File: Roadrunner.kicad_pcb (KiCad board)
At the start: 4 copper layers, 68.6 x 52.1 mm, 100 parts, among them J1 USB_OTG, J10 Digital, J11 ~WAKE, J13 SERIAL 4, J14 SERIAL 3, J15 -AREF, J16 +AREF, J17 SPI 2 (D22,D23), J19 SERIAL 2, J2 JTAG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

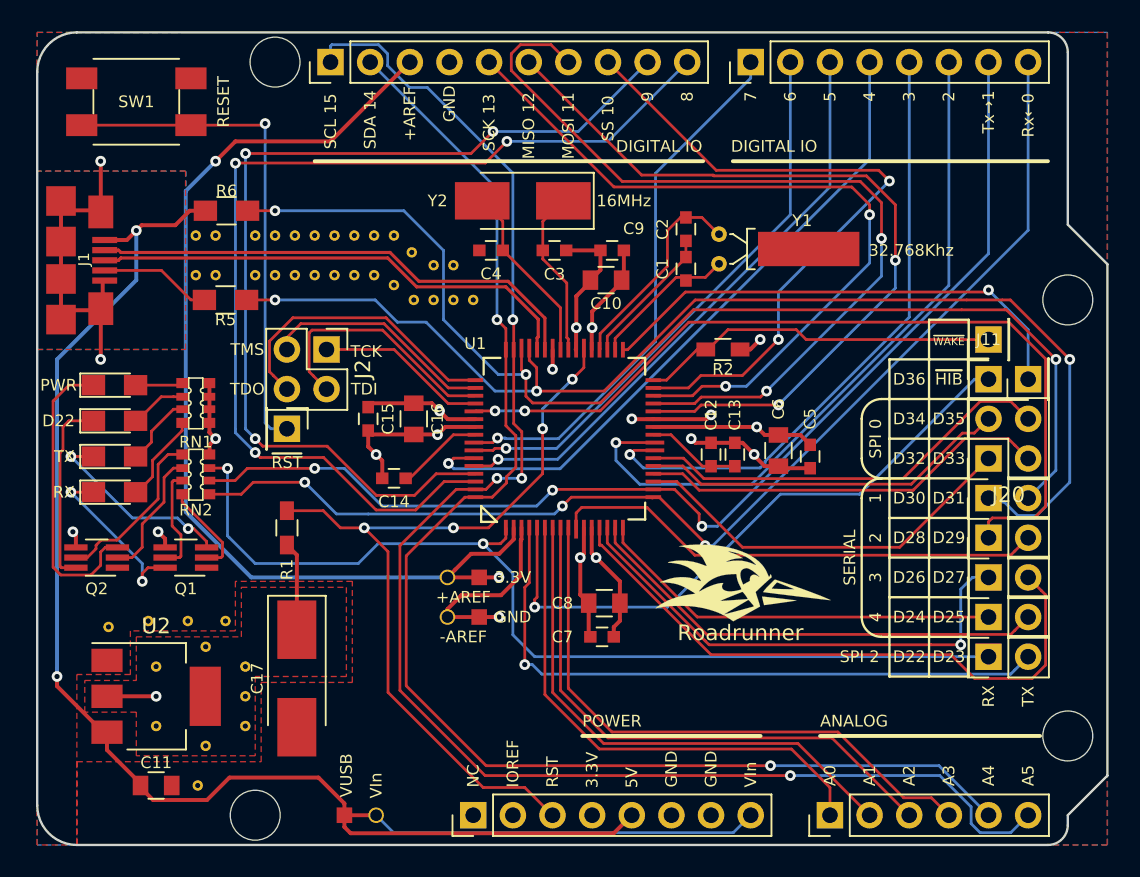
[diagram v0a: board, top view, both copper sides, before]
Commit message: Renaming project ro Roadrunner
Also include various routing changes and a new logo
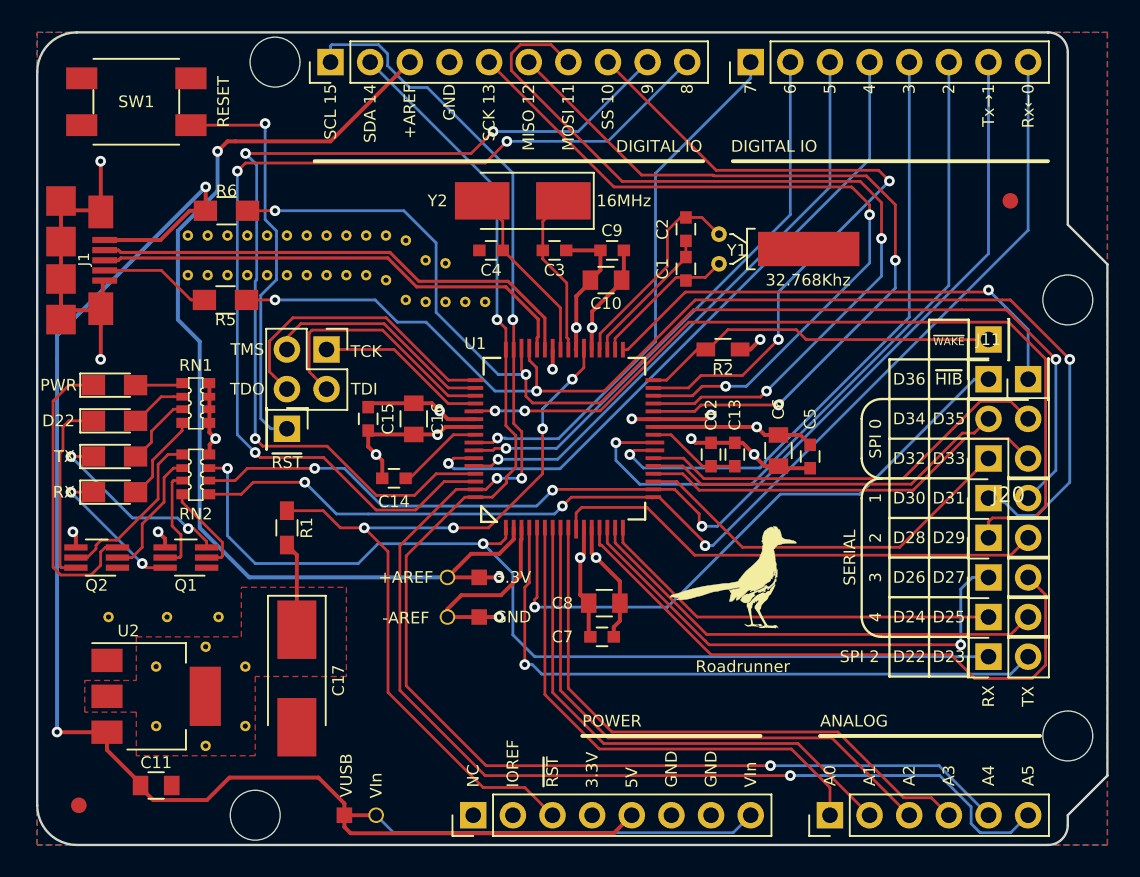
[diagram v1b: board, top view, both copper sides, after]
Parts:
- removed G***: LOGO, Custom-Mounting-Holes:My_Roadrunner
- removed G***: LOGO, Custom-Mounting-Holes:My_Roadrunner_smaller
- removed the REF** at (120.7, 111.4)
- removed the REF** at (127.5, 86.7)
- removed the REF** at (126.2, 89.2)
- removed the REF** at (123.1, 111.4)
- removed the REF** at (121.3, 121.9)
- removed the REF** at (124.3, 116.2)
- added REF**: Fiducial_1mm_Dia_2.54mm_Outer_CopperTop, Fiducials:Fiducial_1mm_Dia_2.54mm_Outer_CopperTop, F.Cu at (173.4, 84.5)
- added REF**: VIA-0.33mm, Custom-Mounting-Holes:VIA-0.33mm, F.Cu at (122.6, 111.1)
- added REF**: VIA-0.33mm, Custom-Mounting-Holes:VIA-0.33mm, F.Cu at (124.5, 86.7)
- added REF**: VIA-0.33mm, Custom-Mounting-Holes:VIA-0.33mm, F.Cu at (123.2, 86.7)
- added REF**: Fiducial_1mm_Dia_2.54mm_Outer_CopperTop, Fiducials:Fiducial_1mm_Dia_2.54mm_Outer_CopperTop, F.Cu at (113.7, 123.2)
- added REF**: VIA-0.33mm, Custom-Mounting-Holes:VIA-0.33mm, F.Cu at (123.2, 89.2)
- added REF**: VIA-0.33mm, Custom-Mounting-Holes:VIA-0.33mm, F.Cu at (124.5, 89.2)
- added REF**: VIA-0.33mm, Custom-Mounting-Holes:VIA-0.33mm, F.Cu at (139.7, 90.9)
- added RoadrunnerLogoMedium: G***, Project-Symbols_Local:RoadrunnerLogoMedium, B.Cu at (128.9, 99.7)
- added RoadrunnerLogoSmall: G***, Project-Symbols_Local:RoadrunnerLogoSmall, F.Cu at (155.6, 108.6)
- moved REF** 1.23 mm to (119.3, 111.1)
- moved REF** 0.85 mm to (134.6, 87.0)
- moved REF** 0.76 mm to (125.7, 86.7)
- moved REF** 0.76 mm to (125.7, 89.2)
- moved REF** 0.76 mm to (127.0, 86.7)
- moved REF** 0.64 mm to (115.6, 111.1)
- moved REF** 0.60 mm to (133.3, 89.5)
- moved REF** 0.60 mm to (135.9, 88.3)
- moved REF** 0.52 mm to (137.2, 88.5)
- moved REF** 0.52 mm to (137.2, 90.9)
- moved REF** 0.52 mm to (135.9, 90.9)
- moved REF** 0.52 mm to (138.4, 90.9)
- moved REF** 0.51 mm to (129.5, 86.7)
- moved REF** 0.51 mm to (130.8, 89.2)
- moved REF** 0.51 mm to (133.3, 86.7)
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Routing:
- net +5V: track 83.5 -> 91.7 mm
- net /~RST: track 85.5 -> 79.4 mm
- net +3V3: track 51.3 -> 48.1 mm, vias 9 -> 8
- net /Q1D1: track 11.3 -> 9.49 mm
- net /+AREF: track 62.9 -> 63.6 mm
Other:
- board text added: "Roadrunner Rev 1.1.2 (Jacob Miller 2017)"
- board text added: "~RST"
- board text removed: "RST"
- board text removed: "Roadrunner Rev 1.1 (Jacob Miller 2017)"

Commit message: Added additional 3.3V x4 and GND x4 headers to rear of board
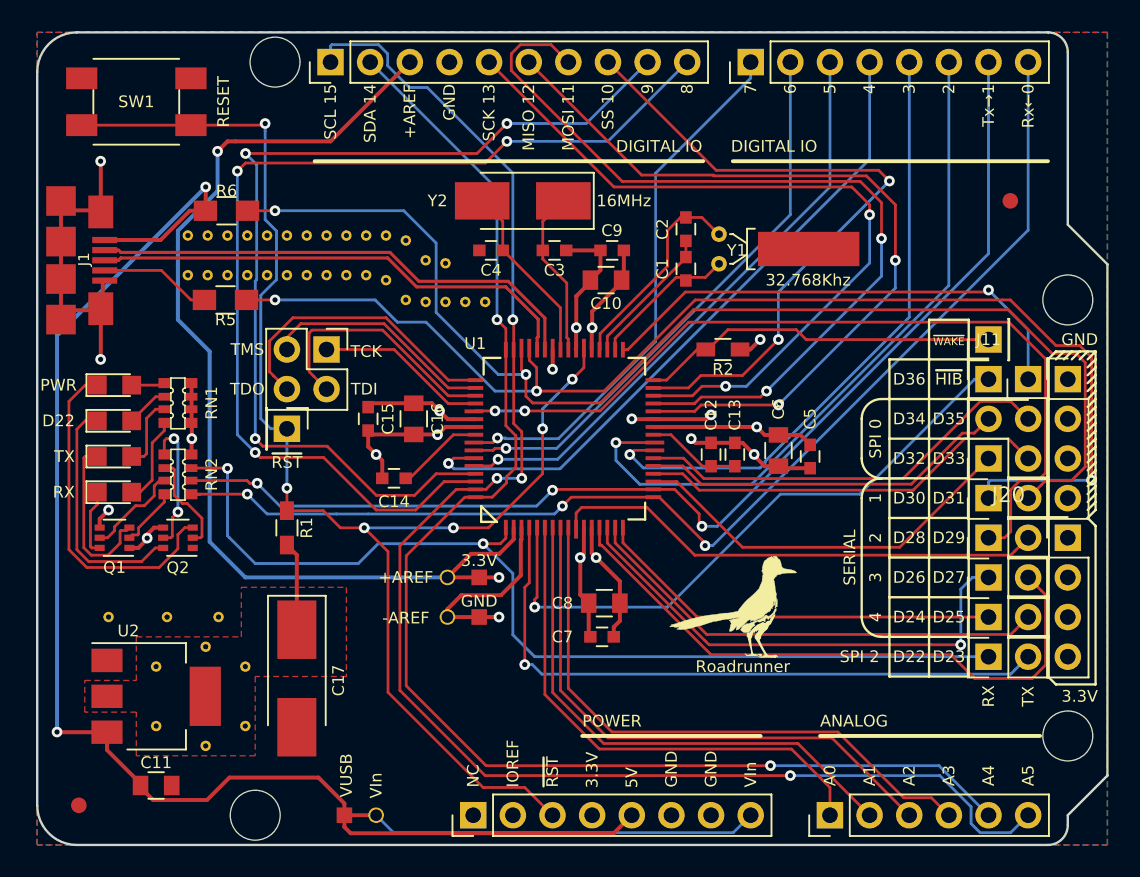
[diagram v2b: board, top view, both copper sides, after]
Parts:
- added J12: Power, Socket_Strips:Socket_Strip_Straight_1x04_Pitch2.54mm, F.Cu at (177.0, 106.0)
- added J18: Ground, Socket_Strips:Socket_Strip_Straight_1x04_Pitch2.54mm, F.Cu at (177.0, 95.9)
- D2, D3, D4, D5: footprint LEDs:LED_0805_HandSoldering -> LEDs:LED_0805
- Q1, Q2: footprint TO_SOT_Packages_SMD:SOT-363_SC-70-6_Handsoldering -> TO_SOT_Packages_SMD:SOT-363_SC-70-6
- moved REF*** 30.8 mm to (116.2, 88.3)
- moved Q2 5.36 mm to (120.0, 106.0)
- moved Q1 4.75 mm to (116.0, 106.0)
- moved RoadrunnerLogoSmall 1.91 mm to (155.6, 110.5)
- moved RN1 1.14 mm to (120.0, 97.4)
- moved RN2 1.14 mm to (120.0, 102.0)
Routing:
- net /~RST: track 79.4 -> 91.6 mm, vias 5 -> 6
- net /Q1D1: track 9.49 -> 4.29 mm, vias 2 -> 0
- net /PB1(U1TX): track 75.4 -> 78.9 mm, vias 3 -> 2
- net /Q2D1: track 12.2 -> 15.5 mm
- net /PB0(U1RX): track 76.4 -> 79.3 mm
- net /Q2D2: track 19.2 -> 21.7 mm
- net /Q2G2: track 11.0 -> 8.70 mm, vias 0 -> 2
- net /Q1G1: track 6.10 -> 3.92 mm
- net GNDREF: track 65.4 -> 67.3 mm
- net /Q1D2: track 12.8 -> 11.0 mm, vias 2 -> 0
- net /Q2G1: track 8.32 -> 6.51 mm
- net /PB6(MISO): track 63.4 -> 64.6 mm
- net /D0(RX): track 74.7 -> 75.7 mm
- net /PWR_LED: track 3.04 -> 2.14 mm
- net /PB6_LED: track 3.62 -> 2.73 mm
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
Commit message: Sweeping changes to board layout.
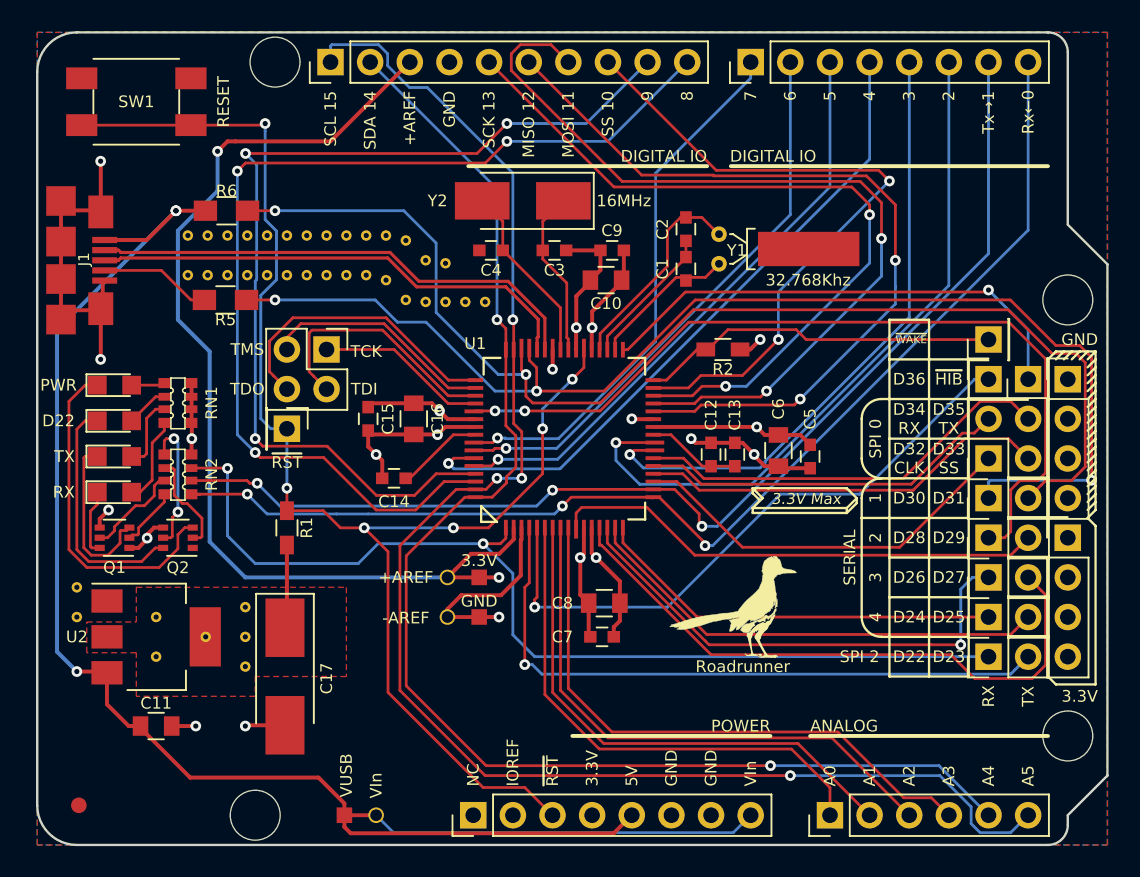
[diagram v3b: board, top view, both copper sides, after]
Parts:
- removed the REF** at (173.4, 84.5)
- removed the REF** at (115.6, 111.1)
- moved REF** 9.28 mm to (113.5, 109.2)
- moved REF** 9.25 mm to (124.3, 110.5)
- moved REF** 6.98 mm to (118.6, 111.1)
- moved REF** 5.78 mm to (113.5, 111.1)
- moved C11 3.81 mm to (118.6, 118.1)
- moved REF** 3.81 mm to (124.3, 114.3)
- moved U2 3.81 mm to (118.6, 112.4)
- moved REF** 1.91 mm to (124.3, 112.4)
- moved C17 0.77 mm to (126.9, 114.9)
- moved REF** 0.64 mm to (121.8, 112.4)
- moved REF** 0.63 mm to (118.6, 113.7)
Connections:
- net /PA2 renamed /SSI_CLK_0
- net /PA3 renamed /SSI_SS_0
- net /PA4 renamed /SSI_RX_0
- net /PA5 renamed /SSI_TX_0
- J7 pad 1: (no net) -> Net-(J7-Pad1)
- U1 pad 28: /12(MISO) -> /D12_RX_1
- U1 pad 29: /11(MOSI) -> /D11_TX_1
- U1 pad 30: /13(SCK) -> /D13_CLK_1
- U1 pad 31: /10(SS) -> /D10_SS_1
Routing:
- net /D12_RX_1: track 0.00 -> 9.20 mm
- net /12(MISO): track 51.4 -> 42.9 mm
- net +5V: track 91.7 -> 83.8 mm, vias 2 -> 3
- net /D11_TX_1: track 0.00 -> 7.05 mm
- net /11(MOSI): track 55.4 -> 48.3 mm
- net /D13_CLK_1: track 0.00 -> 6.21 mm, vias 0 -> 1
- net /13(SCK): track 49.3 -> 43.1 mm, vias 2 -> 1
- net /10(SS): track 43.6 -> 37.6 mm
- net /D10_SS_1: track 0.00 -> 6.04 mm
- net +3V3: track 47.8 -> 47.2 mm
- net GNDREF: track 67.3 -> 67.6 mm, vias 13 -> 14
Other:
- board text added: "3.3V Max"
- board text added: "D30~"
- board text added: "D32 CLK"
- board text added: "D33 SS"
- board text added: "D34 RX"
- board text added: "D35 TX"
- board text added: "Roadrunner Rev 1.2 Jacob Miller - 2017"
- board text removed: "D30"
- board text removed: "D32"
- board text removed: "D33"
- board text removed: "D34"
- board text removed: "D35"
- board text removed: "Roadrunner Rev 1.1.2 (Jacob Miller 2017)"

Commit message: Swapped some 3.3v outputs on rear header for 5V.
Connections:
- J12 pad 3: +3V3 -> +5V
- J12 pad 4: +3V3 -> +5V
- U2 pad 4: +3V3 -> (no net)
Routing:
- net +5V: track 83.8 -> 118.5 mm
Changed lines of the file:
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@@
   (general
     (thickness 1.6)
-    (drawings 207)
-    (tracks 808)
+    (drawings 261)
+    (tracks 813)
     (zones 0)
     (modules 102)
@@
     (44 Edge.Cuts user)
     (45 Margin user)
-    (46 B.CrtYd user)
-    (47 F.CrtYd user)
+    (46 B.CrtYd user hide)
+    (47 F.CrtYd user hide)
     (48 B.Fab user)
     (49 F.Fab user)
@@
     (fp_line (start 1.85 -3.35) (end 1.85 3.35) (layer F.Fab) (width 0.1))
     (pad 4 smd rect (at 3.15 0) (size 2 3.8) (layers Top F.Paste F.Mask)
-      (net 3 +3V3) (zone_connect 2))
+      (zone_connect 2))
     (pad 2 smd rect (at -3.15 0) (size 2 1.5) (layers Top F.Paste F.Mask)
       (net 3 +3V3) (zone_connect 2))
@@
       (net 3 +3V3))
     (pad 3 thru_hole oval (at 0 5.08) (size 1.7 1.7) (drill 1) (layers *.Cu *.Mask)
-      (net 3 +3V3))
+      (net 5 +5V))
     (pad 4 thru_hole oval (at 0 7.62) (size 1.7 1.7) (drill 1) (layers *.Cu *.Mask)
-      (net 3 +3V3))
+      (net 5 +5V))
     (model ${KISYS3DMOD}/Socket_Strips.3dshapes/Socket_Strip_Straight_1x04_Pitch2.54mm.wrl
       (offset (xyz 0 -3.809999942779541 0))
@@
     )
   )
+  (gr_line (start 167.767 117.475) (end 167.894 117.475) (layer F.SilkS) (width 0.15))
+  (gr_line (start 167.767 118.745) (end 167.767 117.475) (layer F.SilkS) (width 0.15))
+  (gr_line (start 174.498 118.745) (end 167.767 118.745) (layer F.SilkS) (width 0.15))
+  (gr_line (start 174.498 117.475) (end 174.498 118.745) (layer F.SilkS) (width 0.15))
+  (gr_line (start 167.894 117.475) (end 174.498 117.475) (layer F.SilkS) (width 0.15))
+  (gr_line (start 176.784 115.824) (end 176.784 116.332) (layer F.SilkS) (width 0.15))
+  (gr_line (start 176.784 115.824) (end 176.276 115.824) (layer F.SilkS) (width 0.15))
+  (gr_line (start 174.498 118.11) (end 176.784 115.824) (layer F.SilkS) (width 0.15))
+  (gr_line (start 171.704 117.856) (end 171.704 118.364) (layer F.SilkS) (width 0.15))
+  (gr_line (start 170.942 118.364) (end 170.942 117.856) (layer F.SilkS) (width 0.15))
+  (gr_line (start 171.704 118.364) (end 170.942 118.364) (layer F.SilkS) (width 0.15))
+  (gr_line (start 170.942 117.856) (end 171.704 117.856) (layer F.SilkS) (width 0.15))
+  (gr_text 5V (at 169.672 118.11) (layer F.SilkS)
+    (effects (font (size 0.75 0.75) (thickness 0.15)))
+  )
+  (gr_line (start 168.021 118.11) (end 168.783 118.11) (layer F.SilkS) (width 0.15))
+  (gr_line (start 168.021 118.364) (end 168.021 117.856) (layer F.SilkS) (width 0.15))
+  (gr_line (start 168.783 118.364) (end 168.021 118.364) (layer F.SilkS) (width 0.15))
+  (gr_line (start 168.783 117.856) (end 168.783 118.364) (layer F.SilkS) (width 0.15))
+  (gr_line (start 168.021 117.856) (end 168.783 117.856) (layer F.SilkS) (width 0.15))
+  (gr_line (start 168.148 118.364) (end 168.656 117.856) (layer F.SilkS) (width 0.15))
+  (gr_line (start 168.656 118.364) (end 168.148 117.856) (layer F.SilkS) (width 0.15))
+  (gr_line (start 178.816 109.855) (end 178.308 110.363) (layer F.SilkS) (width 0.15))
+  (gr_line (start 178.308 109.855) (end 178.816 109.855) (layer F.SilkS) (width 0.15))
+  (gr_line (start 178.562 115.189) (end 178.562 110.109) (layer F.SilkS) (width 0.15))
+  (gr_line (start 176.022 115.189) (end 178.562 115.189) (layer F.SilkS) (width 0.15))
+  (gr_line (start 178.816 110.871) (end 178.308 110.363) (layer F.SilkS) (width 0.15))
+  (gr_line (start 178.308 111.379) (end 178.816 110.871) (layer F.SilkS) (width 0.15))
+  (gr_line (start 178.816 111.887) (end 178.308 111.379) (layer F.SilkS) (width 0.15))
+  (gr_line (start 178.308 112.395) (end 178.816 111.887) (layer F.SilkS) (width 0.15))
+  (gr_line (start 178.816 112.903) (end 178.308 112.395) (layer F.SilkS) (width 0.15))
+  (gr_line (start 178.308 113.411) (end 178.816 112.903) (layer F.SilkS) (width 0.15))
+  (gr_line (start 178.816 113.919) (end 178.308 113.411) (layer F.SilkS) (width 0.15))
+  (gr_line (start 178.308 114.427) (end 178.816 113.919) (layer F.SilkS) (width 0.15))
+  (gr_line (start 178.816 114.935) (end 178.308 114.427) (layer F.SilkS) (width 0.15))
+  (gr_line (start 178.308 115.443) (end 178.816 114.935) (layer F.SilkS) (width 0.15))
+  (gr_line (start 177.8 114.935) (end 178.308 115.443) (layer F.SilkS) (width 0.15))
+  (gr_line (start 177.292 115.443) (end 177.8 114.935) (layer F.SilkS) (width 0.15))
+  (gr_line (start 176.784 114.935) (end 177.292 115.443) (layer F.SilkS) (width 0.15))
+  (gr_line (start 176.276 115.443) (end 176.784 114.935) (layer F.SilkS) (width 0.15))
+  (gr_line (start 176.784 115.443) (end 176.276 114.935) (layer F.SilkS) (width 0.15))
+  (gr_line (start 177.292 114.935) (end 176.784 115.443) (layer F.SilkS) (width 0.15))
+  (gr_line (start 177.8 115.443) (end 177.292 114.935) (layer F.SilkS) (width 0.15))
+  (gr_line (start 178.308 114.935) (end 177.8 115.443) (layer F.SilkS) (width 0.15))
+  (gr_line (start 178.308 109.855) (end 178.308 104.775) (layer F.SilkS) (width 0.15))
+  (gr_line (start 178.308 114.935) (end 178.816 115.443) (layer F.SilkS) (width 0.15))
+  (gr_line (start 178.816 114.427) (end 178.308 114.935) (layer F.SilkS) (width 0.15))
+  (gr_line (start 178.308 113.919) (end 178.816 114.427) (layer F.SilkS) (width 0.15))
+  (gr_line (start 178.816 113.411) (end 178.308 113.919) (layer F.SilkS) (width 0.15))
+  (gr_line (start 178.308 112.903) (end 178.816 113.411) (layer F.SilkS) (width 0.15))
+  (gr_line (start 178.816 112.395) (end 178.308 112.903) (layer F.SilkS) (width 0.15))
+  (gr_line (start 178.308 111.887) (end 178.816 112.395) (layer F.SilkS) (width 0.15))
+  (gr_line (start 178.816 111.379) (end 178.308 111.887) (layer F.SilkS) (width 0.15))
+  (gr_line (start 178.308 110.871) (end 178.816 111.379) (layer F.SilkS) (width 0.15))
+  (gr_line (start 178.816 110.363) (end 178.308 110.871) (layer F.SilkS) (width 0.15))
+  (gr_line (start 178.308 109.855) (end 178.816 110.363) (layer F.SilkS) (width 0.15))
   (gr_line (start 162.8775 104.14) (end 162.8775 104.4575) (layer F.SilkS) (width 0.15))
   (gr_line (start 163.5125 103.505) (end 163.5125 103.8225) (layer F.SilkS) (width 0.15))
@@
   (gr_line (start 178.816 104.267) (end 178.816 94.107) (layer F.SilkS) (width 0.15))
   (gr_line (start 178.308 104.775) (end 178.816 104.267) (layer F.SilkS) (width 0.15))
-  (gr_text 3.3V (at 177.8 116.205) (layer F.SilkS)
+  (gr_text 3.3V (at 173.101 118.11) (layer F.SilkS)
     (effects (font (size 0.75 0.75) (thickness 0.15)))
   )
@@
   (gr_line (start 168.148 94.615) (end 168.148 114.935) (layer F.SilkS) (width 0.15))
   (gr_line (start 165.608 112.395) (end 170.688 112.395) (layer F.SilkS) (width 0.15))
-  (gr_line (start 165.608 109.855) (end 170.688 109.855) (layer F.SilkS) (width 0.15))
+  (gr_line (start 165.608 109.855) (end 178.308 109.855) (layer F.SilkS) (width 0.15))
   (gr_line (start 165.608 107.315) (end 170.688 107.315) (layer F.SilkS) (width 0.15))
   (gr_line (start 165.608 104.775) (end 170.688 104.775) (layer F.SilkS) (width 0.15))
@@
     (effects (font (size 0.75 0.75) (thickness 0.15)))
   )
-  (gr_line (start 160.528 118.745) (end 175.768 118.745) (layer F.SilkS) (width 0.25))
-  (gr_text ANALOG (at 160.528 118.11) (layer F.SilkS)
+  (gr_line (start 160.528 120.015) (end 175.768 120.015) (layer F.SilkS) (width 0.25))
+  (gr_text ANALOG (at 160.528 119.38) (layer F.SilkS)
     (effects (font (size 0.75 0.75) (thickness 0.15)) (justify left))
   )
@@
   (segment (start 115.8 86.965) (end 115.951 86.965) (width 0.254) (layer Top) (net 5) (status 30))
   (segment (start 115.951 86.965) (end 115.197 86.965) (width 0.254) (layer Top) (net 5) (status 30))
+  (segment (start 149.098 123.825) (end 156.793 116.13) (width 0.254) (layer Bottom) (net 5))
+  (segment (start 174.573 116.13) (end 177.038 113.665) (width 0.254) (layer Bottom) (net 5))
+  (segment (start 156.793 116.13) (end 174.573 116.13) (width 0.254) (layer Bottom) (net 5))
+  (segment (start 177.038 112.327081) (end 177.038 113.665) (width 0.254) (layer Bottom) (net 5))
+  (segment (start 177.038 111.125) (end 177.038 112.327081) (width 0.254) (layer Bottom) (net 5))
   (segment (start 161.798 123.825) (end 161.798 122.052891) (width 0.1778) (layer Top) (net 6) (status 10))
   (segment (start 161.798 122.052891) (end 159.328331 119.583222) (width 0.1778) (layer Top) (net 6))
